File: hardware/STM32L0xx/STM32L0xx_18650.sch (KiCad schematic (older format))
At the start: 50 parts, among them J1 SW Debug, J2 Battery, J3 GPIO, J4 USB_B_Micro, J5 Power, J6 LEDs, J7 GPIO, Q1 BSS806N, Q2 BSS806N, Q3 BSS806N, Q4 BSS806N, SW1 Mode, SW2 Power, U1 STM32L072KZTx, U2 AP2210N-3.3TRG1, U3 MCP73833-AMI_UN, Y1 32.768kHz

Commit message: Move JTAG to GPIOs
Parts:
- removed J1: SW Debug, Connector_PinHeader_1.27mm:PinHeader_2x05_P1.27mm_Vertical, symbol Connector:Conn_ARM_JTAG_SWD_10
- D4, D5, D7, D8: value LED_Small -> LED
- J7: footprint Connector_PinHeader_2.54mm:PinHeader_1x05_P2.54mm_Vertical -> Connector_PinHeader_2.54mm:PinHeader_1x08_P2.54mm_Vertical; symbol Connector_Generic:Conn_01x05 -> Connector_Generic:Conn_01x08
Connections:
- net labels added: PA13, PA14
- net labels removed: SWCLK, SWDIO
- wire segments 198 -> 191
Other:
- note removed: "JTAG / SWD"
- moved on the sheet: J3, J5, U2
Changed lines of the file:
@@
 P 8550 1400
 F 0 "D5" H 8550 1500 50  0000 C CNN
-F 1 "LED_Small" H 8550 1544 50  0001 C CNN
+F 1 "LED" H 8550 1544 50  0001 C CNN
 F 2 "LED_SMD:LED_0603_1608Metric" V 8550 1400 50  0001 C CNN
 F 3 "~" V 8550 1400 50  0001 C CNN
@@
 P 7650 1400
 F 0 "D4" H 7650 1500 50  0000 C CNN
-F 1 "LED_Small" H 7650 1544 50  0001 C CNN
+F 1 "LED" H 7650 1544 50  0001 C CNN
 F 2 "LED_SMD:LED_0603_1608Metric" V 7650 1400 50  0001 C CNN
 F 3 "~" V 7650 1400 50  0001 C CNN
@@
 P 9450 1400
 F 0 "D7" H 9450 1500 50  0000 C CNN
-F 1 "LED_Small" H 9450 1544 50  0001 C CNN
+F 1 "LED" H 9450 1544 50  0001 C CNN
 F 2 "LED_SMD:LED_0603_1608Metric" V 9450 1400 50  0001 C CNN
 F 3 "~" V 9450 1400 50  0001 C CNN
@@
 P 10250 1400
 F 0 "D8" H 10250 1500 50  0000 C CNN
-F 1 "LED_Small" H 10250 1544 50  0001 C CNN
+F 1 "LED" H 10250 1544 50  0001 C CNN
 F 2 "LED_SMD:LED_0603_1608Metric" V 10250 1400 50  0001 C CNN
 F 3 "~" V 10250 1400 50  0001 C CNN
@@
 	4800 4000 4950 4000
 Text Label 4950 4100 0    50   ~ 0
-SWCLK
+PA14
 Text Label 4950 4000 0    50   ~ 0
-SWDIO
-Text Label 1050 6000 0    50   ~ 0
+PA13
+Text Label 1000 5450 0    50   ~ 0
 PB5
-Text Label 1050 5900 0    50   ~ 0
+Text Label 1000 5350 0    50   ~ 0
 PB6
-Text Label 1050 6200 0    50   ~ 0
+Text Label 1000 5850 0    50   ~ 0
 PA9
-Text Label 1050 6100 0    50   ~ 0
+Text Label 1000 5750 0    50   ~ 0
 PA10
 Wire Wire Line
-	2050 5250 1850 5250
-Wire Wire Line
-	2050 5150 2050 5250
+	2750 5450 2550 5450
+Wire Wire Line
+	2750 5350 2750 5450
 $Comp
 L power:+BATT #PWR?
 U 1 1 5C2E47A9
-P 1900 5050
+P 2600 5250
 AR Path="/5BD64BD8/5C2E47A9" Ref="#PWR?"  Part="1"
 AR Path="/5C2E47A9" Ref="#PWR0131"  Part="1"
-F 0 "#PWR0131" H 1900 4900 50  0001 C CNN
-F 1 "+BATT" H 1915 5223 50  0000 C CNN
-F 2 "" H 1900 5050 50  0001 C CNN
-F 3 "" H 1900 5050 50  0001 C CNN
-	1    1900 5050
-	1    0    0    -1
-$EndComp
-Wire Wire Line
-	1900 5150 1850 5150
-Wire Wire Line
-	1900 5050 1900 5150
+F 0 "#PWR0131" H 2600 5100 50  0001 C CNN
+F 1 "+BATT" H 2615 5423 50  0000 C CNN
+F 2 "" H 2600 5250 50  0001 C CNN
+F 3 "" H 2600 5250 50  0001 C CNN
+	1    2600 5250
+	1    0    0    -1
+$EndComp
+Wire Wire Line
+	2600 5350 2550 5350
+Wire Wire Line
+	2600 5250 2600 5350
 $Comp
 L power:+3.3V #PWR0130
 U 1 1 5C2D9A3C
-P 2050 5150
-F 0 "#PWR0130" H 2050 5000 50  0001 C CNN
-F 1 "+3.3V" H 2065 5323 50  0000 C CNN
-F 2 "" H 2050 5150 50  0001 C CNN
-F 3 "" H 2050 5150 50  0001 C CNN
-	1    2050 5150
+P 2750 5350
+F 0 "#PWR0130" H 2750 5200 50  0001 C CNN
+F 1 "+3.3V" H 2765 5523 50  0000 C CNN
+F 2 "" H 2750 5350 50  0001 C CNN
+F 3 "" H 2750 5350 50  0001 C CNN
+	1    2750 5350
 	1    0    0    -1
 $EndComp
@@
 L power:GND #PWR0129
 U 1 1 5C2D8F0C
-P 1850 5450
-F 0 "#PWR0129" H 1850 5200 50  0001 C CNN
-F 1 "GND" H 1855 5277 50  0000 C CNN
-F 2 "" H 1850 5450 50  0001 C CNN
-F 3 "" H 1850 5450 50  0001 C CNN
-	1    1850 5450
+P 2550 5650
+F 0 "#PWR0129" H 2550 5400 50  0001 C CNN
+F 1 "GND" H 2555 5477 50  0000 C CNN
+F 2 "" H 2550 5650 50  0001 C CNN
+F 3 "" H 2550 5650 50  0001 C CNN
+	1    2550 5650
 	1    0    0    -1
 $EndComp
@@
 L Connector_Generic:Conn_01x04 J?
 U 1 1 5C2B93C1
-P 1650 5350
+P 2350 5550
 AR Path="/5BD64BD8/5C2B93C1" Ref="J?"  Part="1"
 AR Path="/5C2B93C1" Ref="J5"  Part="1"
-F 0 "J5" H 1729 5342 50  0000 L CNN
-F 1 "Power" H 1729 5251 50  0000 L CNN
-F 2 "Connector_PinHeader_2.54mm:PinHeader_1x04_P2.54mm_Vertical" H 1650 5350 50  0001 C CNN
-F 3 "~" H 1650 5350 50  0001 C CNN
-	1    1650 5350
+F 0 "J5" H 2429 5542 50  0000 L CNN
+F 1 "Power" H 2429 5451 50  0000 L CNN
+F 2 "Connector_PinHeader_2.54mm:PinHeader_1x04_P2.54mm_Vertical" H 2350 5550 50  0001 C CNN
+F 3 "~" H 2350 5550 50  0001 C CNN
+	1    2350 5550
 	-1   0    0    1
 $EndComp
-$Comp
-L Connector_Generic:Conn_01x05 J?
-U 1 1 5C3E2B10
-P 850 6000
-AR Path="/5BD64BD8/5C3E2B10" Ref="J?"  Part="1"
-AR Path="/5C3E2B10" Ref="J7"  Part="1"
-F 0 "J7" H 929 5992 50  0000 L CNN
-F 1 "GPIO" H 929 5901 50  0000 L CNN
-F 2 "Connector_PinHeader_2.54mm:PinHeader_1x05_P2.54mm_Vertical" H 850 6000 50  0001 C CNN
-F 3 "~" H 850 6000 50  0001 C CNN
-	1    850  6000
-	-1   0    0    1
-$EndComp
-Text Label 1050 5800 0    50   ~ 0
+Text Label 1000 5250 0    50   ~ 0
 PB7
-Text Label 1050 5550 0    50   ~ 0
+Text Label 1750 5700 0    50   ~ 0
 PA8
-Text Label 1050 5450 0    50   ~ 0
+Text Label 1750 5600 0    50   ~ 0
 PA7
-Text Label 1050 5350 0    50   ~ 0
+Text Label 1750 5500 0    50   ~ 0
 PA6
-Text Label 1050 5250 0    50   ~ 0
+Text Label 1750 5400 0    50   ~ 0
 PA5
-Text Label 1050 5150 0    50   ~ 0
+Text Label 1750 5300 0    50   ~ 0
 PA4
-$Comp
-L Connector_Generic:Conn_01x05 J?
-U 1 1 5C29837D
-P 850 5350
-AR Path="/5BD64BD8/5C29837D" Ref="J?"  Part="1"
-AR Path="/5C29837D" Ref="J3"  Part="1"
-F 0 "J3" H 929 5342 50  0000 L CNN
-F 1 "GPIO" H 929 5251 50  0000 L CNN
-F 2 "Connector_PinHeader_2.54mm:PinHeader_1x05_P2.54mm_Vertical" H 850 5350 50  0001 C CNN
-F 3 "~" H 850 5350 50  0001 C CNN
-	1    850  5350
-	-1   0    0    -1
-$EndComp
 Wire Notes Line
 	2350 6500 2350 7700
@@
 Wire Wire Line
 	2800 3350 2800 3450
-Text Label 1850 5350 0    50   ~ 0
+Text Label 2550 5550 0    50   ~ 0
 VUSB
 $Comp
@@
 	0    1    1    0
 $EndComp
-Text Label 4800 6800 0    50   ~ 0
-SWDIO
-Text Label 4800 6700 0    50   ~ 0
-SWCLK
-Text Label 4800 6500 0    50   ~ 0
-RESET
-$Comp
-L power:+3.3V #PWR0104
-U 1 1 5D7E89AF
-P 4300 6200
-F 0 "#PWR0104" H 4300 6050 50  0001 C CNN
-F 1 "+3.3V" H 4315 6373 50  0000 C CNN
-F 2 "" H 4300 6200 50  0001 C CNN
-F 3 "" H 4300 6200 50  0001 C CNN
-	1    4300 6200
-	1    0    0    -1
-$EndComp
-$Comp
-L power:GND #PWR0105
-U 1 1 5D7E99F4
-P 4250 7450
-F 0 "#PWR0105" H 4250 7200 50  0001 C CNN
-F 1 "GND" H 4255 7277 50  0000 C CNN
-F 2 "" H 4250 7450 50  0001 C CNN
-F 3 "" H 4250 7450 50  0001 C CNN
-	1    4250 7450
-	1    0    0    -1
-$EndComp
-Wire Wire Line
-	4200 7400 4200 7450
-Wire Wire Line
-	4200 7450 4250 7450
-Wire Wire Line
-	4250 7450 4300 7450
-Wire Wire Line
-	4300 7450 4300 7400
-Connection ~ 4250 7450
-Wire Wire Line
-	4800 6900 4800 7000
-Wire Wire Line
-	4800 7450 4300 7450
-Connection ~ 4800 7000
-Wire Wire Line
-	4800 7000 4800 7450
-Connection ~ 4300 7450
-Wire Notes Line
-	3850 5950 3850 7700
-Wire Notes Line
-	5100 7700 5100 5950
-Wire Notes Line
-	3850 7700 5100 7700
-Wire Notes Line
-	3850 5950 5100 5950
-Wire Notes Line
-	5200 6650 5200 7700
-Wire Notes Line
-	5200 7700 6450 7700
-Wire Notes Line
-	6450 6650 6450 7700
-Wire Notes Line
-	5200 6650 6450 6650
+Wire Notes Line
+	3750 6650 3750 7700
+Wire Notes Line
+	3750 7700 5000 7700
+Wire Notes Line
+	5000 6650 5000 7700
+Wire Notes Line
+	3750 6650 5000 6650
 $Comp
 L Jeremy:AP2210-3.3TRG1 U2
 U 1 1 5CD3E552
-P 5500 7050
-F 0 "U2" H 5600 6750 50  0000 C CNN
-F 1 "AP2210N-3.3TRG1" H 5775 7234 50  0000 C CNN
-F 2 "Package_TO_SOT_SMD:SOT-23" H 5450 7450 50  0001 C CNN
-F 3 "" H 5450 7450 50  0001 C CNN
-F 4 "AP2210N-3.3TRG1" H 5500 7050 50  0001 C CNN "MPN"
-	1    5500 7050
-	1    0    0    -1
-$EndComp
-Text Notes 5200 6650 0    50   ~ 0
+P 4050 7050
+F 0 "U2" H 4150 6750 50  0000 C CNN
+F 1 "AP2210N-3.3TRG1" H 4325 7234 50  0000 C CNN
+F 2 "Package_TO_SOT_SMD:SOT-23" H 4000 7450 50  0001 C CNN
+F 3 "" H 4000 7450 50  0001 C CNN
+F 4 "AP2210N-3.3TRG1" H 4050 7050 50  0001 C CNN "MPN"
+	1    4050 7050
+	1    0    0    -1
+$EndComp
+Text Notes 3750 6650 0    50   ~ 0
 3.3v Power
 Wire Wire Line
-	6300 7000 6200 7000
-Wire Wire Line
-	6300 6900 6300 7000
-Text Label 5350 7000 2    50   ~ 0
+	4850 7000 4750 7000
+Wire Wire Line
+	4850 6900 4850 7000
+Text Label 3900 7000 2    50   ~ 0
 VIN
 $Comp
 L power:GND #PWR0108
 U 1 1 5BD85B6B
-P 5750 7450
-F 0 "#PWR0108" H 5750 7200 50  0001 C CNN
-F 1 "GND" H 5755 7277 50  0000 C CNN
-F 2 "" H 5750 7450 50  0001 C CNN
-F 3 "" H 5750 7450 50  0001 C CNN
-	1    5750 7450
+P 4300 7450
+F 0 "#PWR0108" H 4300 7200 50  0001 C CNN
+F 1 "GND" H 4305 7277 50  0000 C CNN
+F 2 "" H 4300 7450 50  0001 C CNN
+F 3 "" H 4300 7450 50  0001 C CNN
+	1    4300 7450
 	1    0    0    -1
 $EndComp
@@
 L power:+3V3 #PWR0102
 U 1 1 5BD53A46
-P 6300 6900
-F 0 "#PWR0102" H 6300 6750 50  0001 C CNN
-F 1 "+3V3" H 6315 7073 50  0000 C CNN
-F 2 "" H 6300 6900 50  0001 C CNN
-F 3 "" H 6300 6900 50  0001 C CNN
-	1    6300 6900
-	1    0    0    -1
-$EndComp
-$Comp
-L Connector:Conn_ARM_JTAG_SWD_10 J1
-U 1 1 5D4460E4
-P 4300 6800
-F 0 "J1" H 3950 6200 50  0000 C CNN
-F 1 "SW Debug" H 4550 6250 50  0000 C CNN
-F 2 "Connector_PinHeader_1.27mm:PinHeader_2x05_P1.27mm_Vertical" H 4300 6800 50  0001 C CNN
-F 3 "~" H 4300 6800 50  0001 C CNN
-	1    4300 6800
-	1    0    0    -1
-$EndComp
-Text Notes 3850 5950 0    50   ~ 0
-JTAG / SWD
+P 4850 6900
+F 0 "#PWR0102" H 4850 6750 50  0001 C CNN
+F 1 "+3V3" H 4865 7073 50  0000 C CNN
+F 2 "" H 4850 6900 50  0001 C CNN
+F 3 "" H 4850 6900 50  0001 C CNN
+	1    4850 6900
+	1    0    0    -1
+$EndComp
 Wire Wire Line
 	2800 3450 2850 3450
@@
 	1    0    0    -1
 $EndComp
+Text Label 1000 5650 0    50   ~ 0
+PA13
+Text Label 1000 5550 0    50   ~ 0
+PA14
+Text Label 1000 5150 0    50   ~ 0
+RESET
+$Comp
+L Connector_Generic:Conn_01x05 J?
+U 1 1 5C29837D
+P 1550 5500
+AR Path="/5BD64BD8/5C29837D" Ref="J?"  Part="1"
+AR Path="/5C29837D" Ref="J3"  Part="1"
+F 0 "J3" H 1629 5492 50  0000 L CNN
+F 1 "GPIO" H 1629 5401 50  0000 L CNN
+F 2 "Connector_PinHeader_2.54mm:PinHeader_1x05_P2.54mm_Vertical" H 1550 5500 50  0001 C CNN
+F 3 "~" H 1550 5500 50  0001 C CNN
+	1    1550 5500
+	-1   0    0    -1
+$EndComp
+$Comp
+L Connector_Generic:Conn_01x08 J?
+U 1 1 5C3E2B10
+P 800 5550
+AR Path="/5BD64BD8/5C3E2B10" Ref="J?"  Part="1"
+AR Path="/5C3E2B10" Ref="J7"  Part="1"
+F 0 "J7" H 879 5542 50  0000 L CNN
+F 1 "GPIO" H 879 5451 50  0000 L CNN
+F 2 "Connector_PinHeader_2.54mm:PinHeader_1x08_P2.54mm_Vertical" H 800 5550 50  0001 C CNN
+F 3 "~" H 800 5550 50  0001 C CNN
+	1    800  5550
+	-1   0    0    1
+$EndComp
 $EndSCHEMATC

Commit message: Hardware feedback.
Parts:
- added C12: 2.2uF, Capacitor_SMD:C_0603_1608Metric, symbol Device:C
- added C13, C6: 1.0uf, Capacitor_SMD:C_0603_1608Metric, symbol Device:C
- added U4: TPD2E2U06, Package_TO_SOT_SMD:SOT-553, symbol Power_Protection:TPD2E2U06
- J2: footprint Jeremy:Battery_Clips_18650 -> BatteryClips:Keystone54_18650_PTC
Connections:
- net +3V3: now also C12.1
- net GND: now also C12.2, C13.1, C6.2, U4.4
- net USB_D+: now also U4.3
- net USB_D-: now also U4.5
- net VIN: now also C6.1
- net VUSB: now also C13.2
- no-connect marks 5 -> 7
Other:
- moved on the sheet: D1, J4, U2

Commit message: Change USB TVS.
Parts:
- removed U4: TPD2E2U06, Package_TO_SOT_SMD:SOT-553, symbol Power_Protection:TPD2E2U06
- added U4: ESD7002WTT1G, Package_TO_SOT_SMD:SOT-323_SC-70, symbol Jeremy:ESD7002WTT1G
- D3: MFN Rohm -> (none); MPN SML-D12V1WT86 -> 150060SS75000
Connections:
- net GND: now also U4.3 (GND)
- net USB_D+: now also U4.1
- net USB_D-: now also U4.2
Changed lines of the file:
@@
 F 2 "LED_SMD:LED_0603_1608Metric_Castellated" H 1350 4250 50  0001 C CNN
 F 3 "" H 1350 4250 50  0001 C CNN
-F 4 "Rohm" H 1350 4250 50  0001 C CNN "MFN"
-F 5 "SML-D12V1WT86" H 1350 4250 50  0001 C CNN "MPN"
-F 6 "0603" H 0   0   50  0001 C CNN "Package"
+F 4 "150060SS75000" H 1350 4250 50  0001 C CNN "MPN"
+F 5 "0603" H 0   0   50  0001 C CNN "Package"
 	1    1350 4250
 	-1   0    0    1
@@
 Wire Wire Line
 	2750 7350 2750 7400
-Wire Wire Line
-	3750 7300 3800 7300
-Wire Wire Line
-	3750 7400 3750 7300
-$Comp
-L power:GND #PWR06
-U 1 1 5DBCADF0
-P 3750 7400
-F 0 "#PWR06" H 3750 7150 50  0001 C CNN
-F 1 "GND" H 3755 7227 50  0000 C CNN
-F 2 "" H 3750 7400 50  0001 C CNN
-F 3 "" H 3750 7400 50  0001 C CNN
-	1    3750 7400
-	1    0    0    -1
-$EndComp
-$Comp
-L Power_Protection:TPD2E2U06 U4
-U 1 1 5DB8930A
-P 4100 7300
-F 0 "U4" V 4054 7530 50  0000 L CNN
-F 1 "TPD2E2U06" V 4145 7530 50  0000 L CNN
-F 2 "Package_TO_SOT_SMD:SOT-553" H 3300 7050 50  0001 C CNN
-F 3 "http://www.ti.com/lit/ds/symlink/tpd2e2u06.pdf" H 3900 7500 50  0001 C CNN
-F 4 "TPD2E2U06DRLR" H 4100 7300 50  0001 C CNN "MPN"
-F 5 "SOT-553" H 4100 7300 50  0001 C CNN "Package"
-	1    4100 7300
-	0    1    1    0
-$EndComp
 Wire Notes Line
 	4650 6350 4650 7700
@@
 $EndComp
 Wire Wire Line
-	3100 6950 4000 6950
-Wire Wire Line
-	3100 6850 4200 6850
-Wire Wire Line
-	4000 7000 4000 6950
-Connection ~ 4000 6950
-Wire Wire Line
-	4200 7000 4200 6950
-Wire Wire Line
-	4200 6950 4200 6850
-Wire Wire Line
-	4200 6850 4300 6850
-Connection ~ 4200 6850
-Wire Wire Line
-	4000 6950 4300 6950
-Wire Wire Line
 	3300 6650 3450 6650
 Wire Wire Line
@@
 Wire Wire Line
 	3450 7350 3450 7400
-NoConn ~ 4000 7600
-NoConn ~ 4200 7600
+$Comp
+L power:GND #PWR06
+U 1 1 5DBCADF0
+P 4550 7450
+F 0 "#PWR06" H 4550 7200 50  0001 C CNN
+F 1 "GND" H 4555 7277 50  0000 C CNN
+F 2 "" H 4550 7450 50  0001 C CNN
+F 3 "" H 4550 7450 50  0001 C CNN
+	1    4550 7450
+	1    0    0    -1
+$EndComp
+Wire Wire Line
+	4550 7300 4550 7450
+Wire Wire Line
+	3100 6850 3750 6850
+Wire Wire Line
+	3100 6950 3800 6950
+$Comp
+L Jeremy:ESD7002WTT1G U4
+U 1 1 5DA9EA0D
+P 4200 7300
+F 0 "U4" H 4450 7200 50  0000 C CNN
+F 1 "ESD7002WTT1G" H 4300 7450 50  0000 C CNN
+F 2 "Package_TO_SOT_SMD:SOT-323_SC-70" H 4200 7600 50  0001 C CNN
+F 3 "https://www.onsemi.com/pub/Collateral/ESD7002-D.PDF" H 4050 7300 50  0001 C CNN
+F 4 "SC-70, SOT-323" H 4200 7300 50  0001 C CNN "Package"
+F 5 "ESD7002WTT1G" H 4200 7300 50  0001 C CNN "MPN"
+	1    4200 7300
+	1    0    0    -1
+$EndComp
+Wire Wire Line
+	3850 7250 3750 7250
+Wire Wire Line
+	3750 7250 3750 6850
+Connection ~ 3750 6850
+Wire Wire Line
+	3750 6850 4300 6850
+Wire Wire Line
+	3850 7350 3800 7350
+Wire Wire Line
+	3800 7350 3800 6950
+Connection ~ 3800 6950
+Wire Wire Line
+	3800 6950 4300 6950
+NoConn ~ 9350 5250
+NoConn ~ 9350 5350
 $EndSCHEMATC

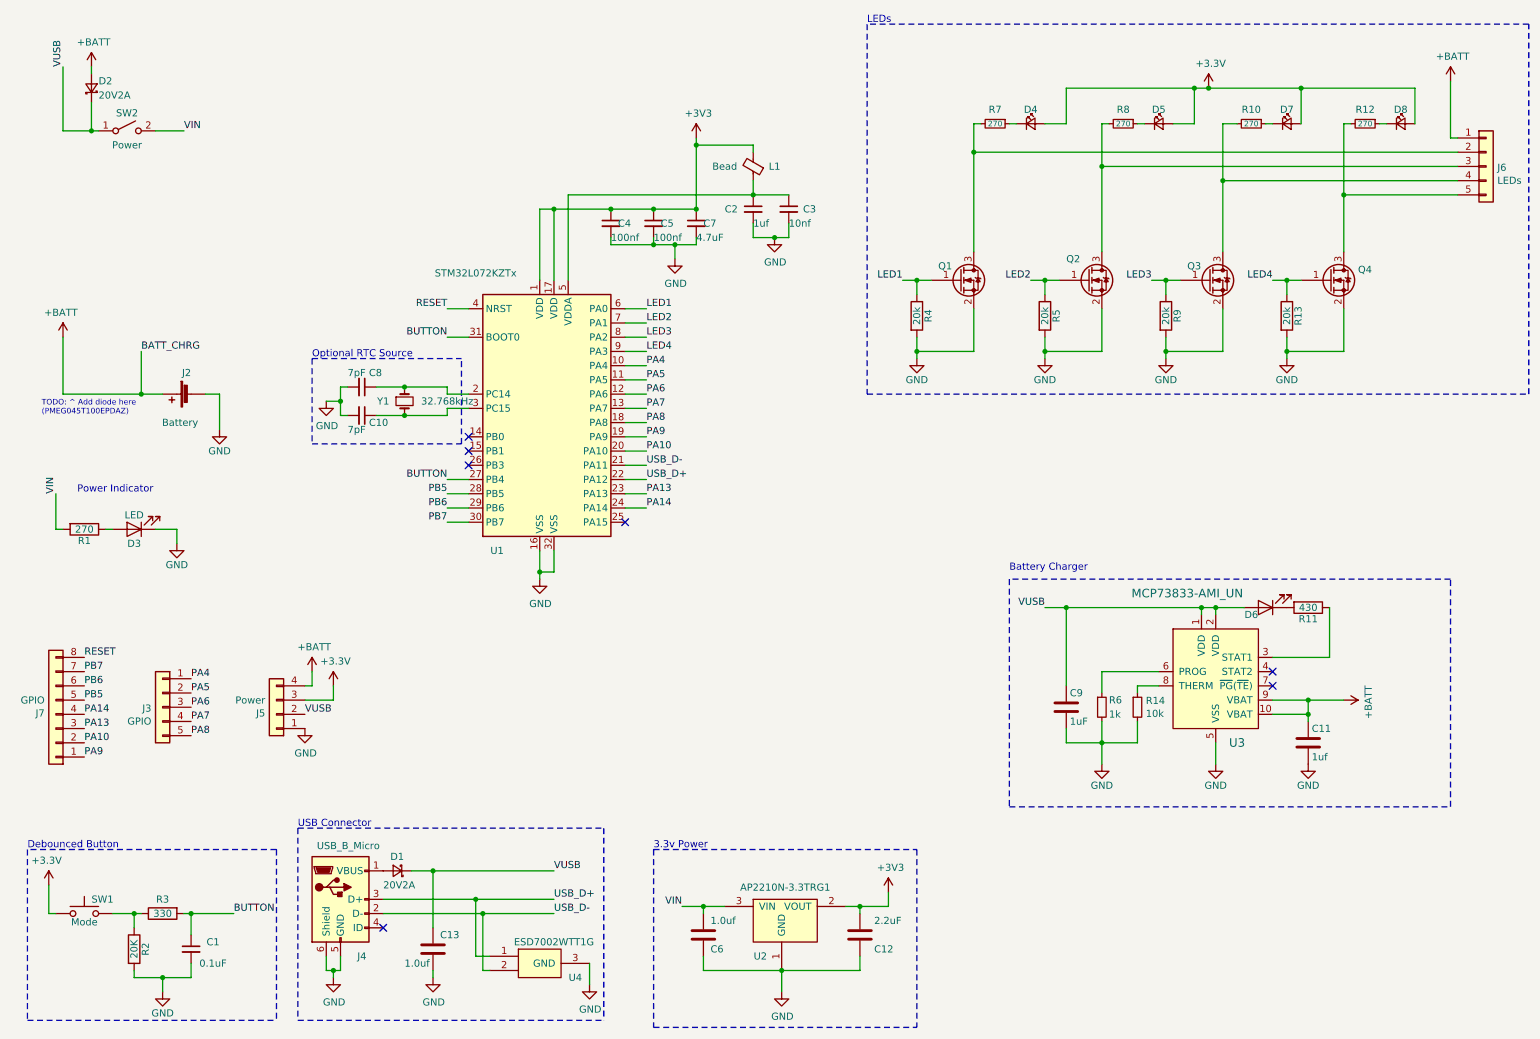
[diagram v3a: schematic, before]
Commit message: Change battery changing controller
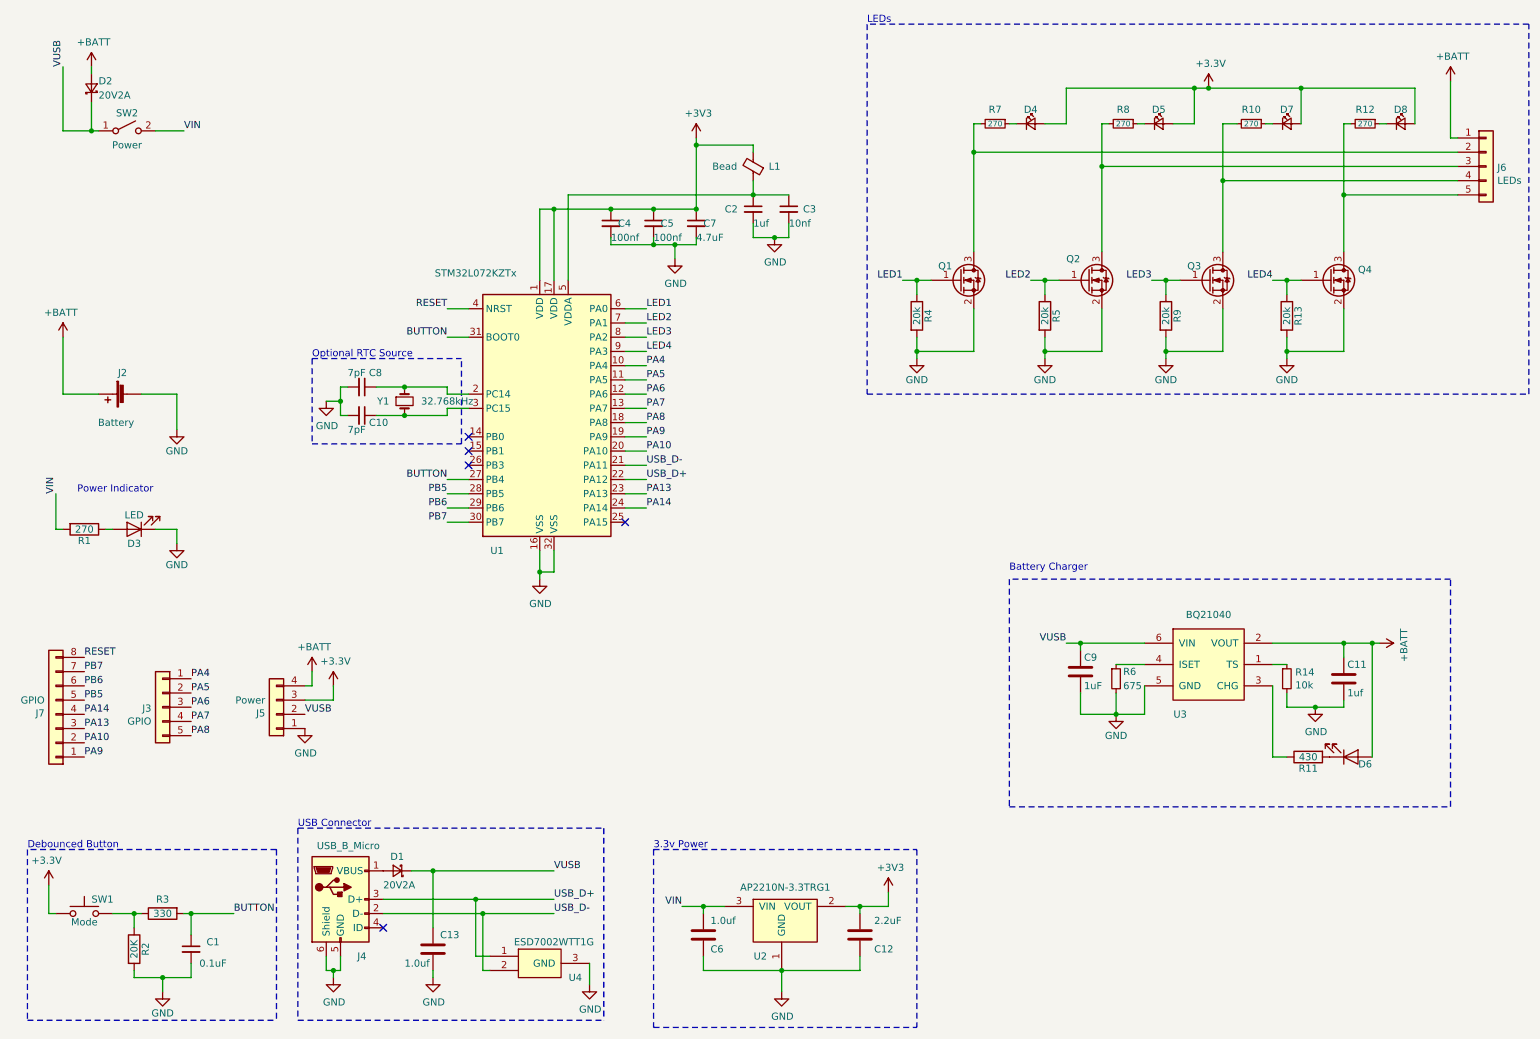
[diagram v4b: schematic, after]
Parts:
- removed U3: MCP73833-AMI_UN, Package_SO:TSSOP-10_3x3mm_P0.5mm, symbol dk_PMIC-Battery-Chargers:MCP73833-AMI_UN
- added U3: BQ21040, Package_TO_SOT_SMD:SOT-23-6, symbol Jeremy:BQ21040
- D6: footprint LED_SMD:LED_0603_1608Metric_Castellated -> LED_SMD:LED_0603_1608Metric
- R6: value 1k -> 675
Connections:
- net +BATT: now also D6.2 (A), U3.2 (VOUT)
- net GND: now also U3.5 (GND)
- net VUSB: now also U3.6 (VIN); no longer D6.2 (A)
- net at R11.1: now also U3.3 (CHG)
- net at R6.1: now also U3.4 (ISET)
- net at R14.1: now also U3.1 (TS)
- no-connect marks 7 -> 5
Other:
- note removed: "TODO: ^ Add diode here\n(PMEG045T100EPDAZ)"
- moved on the sheet: J2
